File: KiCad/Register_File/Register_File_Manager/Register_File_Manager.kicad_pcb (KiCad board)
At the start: 2 copper layers, 100 x 100 mm, 39 parts, among them J1 Conn_01x04_Socket, J10 Conn_01x02_Socket, J11 Conn_01x02_Socket, J12 Conn_01x02_Socket, J13 Conn_01x02_Socket, J14 Conn_01x02_Socket, J15 Conn_01x02_Socket, J16 Conn_01x02_Socket, J17 Conn_01x02_Socket, J18 Conn_01x02_Socket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

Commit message: finished registier file boards
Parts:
- removed D0, D5, D6, D7: LED, LED_THT:LED_Rectangular_W3.0mm_H2.0mm
- removed RN1: R_Network08_US, Resistor_THT:R_Array_SIP9
- added J21: Conn_01x08_Socket, Connector_PinHeader_2.54mm:PinHeader_1x08_P2.54mm_Vertical, F.Cu at (142.3, 76.5)
- added J22: Conn_01x08_Socket, Connector_PinHeader_2.54mm:PinHeader_1x08_P2.54mm_Vertical, F.Cu at (177.4, 76.5)
- added J23: Conn_01x08_Socket, Connector_PinHeader_2.54mm:PinHeader_1x08_P2.54mm_Vertical, F.Cu at (142.9, 100.5)
- added J24: Conn_01x08_Socket, Connector_PinHeader_2.54mm:PinHeader_1x08_P2.54mm_Vertical, F.Cu at (176.1, 100.5)
- added R1: 1k, Resistor_SMD:R_1206_3216Metric_Pad1.30x1.75mm_HandSolder, F.Cu at (172.0, 60.5)
- added R2: 1k, Resistor_SMD:R_1206_3216Metric_Pad1.30x1.75mm_HandSolder, F.Cu at (176.0, 60.5)
- added R3: 1k, Resistor_SMD:R_1206_3216Metric_Pad1.30x1.75mm_HandSolder, F.Cu at (180.0, 60.5)
- added R4: 1k, Resistor_SMD:R_1206_3216Metric_Pad1.30x1.75mm_HandSolder, F.Cu at (184.0, 60.5)
- added SW1: SW_SPDT, Button_Switch_THT:SW_Slide_SPDT_Angled_CK_OS102011MA1Q, F.Cu at (117.5, 54.0)
- added U7: 74LS245, Package_DIP:DIP-20_W7.62mm_Socket_LongPads, F.Cu at (134.4, 63.8)
- moved D4 36.1 mm to (184.0, 54.0), turned to -90 degrees
- moved D3 24.6 mm to (180.0, 54.0), turned to -90 degrees
- moved U3 20.6 mm to (157.1, 87.8), turned to 90 degrees
- moved U5 16.0 mm to (155.8, 111.8), turned to 90 degrees
- moved J1 14.5 mm to (147.0, 142.0)
- moved J2 14.5 mm to (161.5, 142.0)
- moved D2 13.2 mm to (176.0, 54.0), turned to -90 degrees
- moved U2 12.9 mm to (122.0, 87.8), turned to 90 degrees
- moved U4 12.3 mm to (122.5, 111.8), turned to 90 degrees
- moved U1 7.07 mm to (155.6, 130.8)
- moved D1 2.50 mm to (172.0, 54.0), turned to -90 degrees
- moved U6 1.43 mm to (125.4, 131.2)
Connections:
- net /SELECTED_REG_0 renamed SELECTED_REG_0
- net /SELECTED_REG_1 renamed SELECTED_REG_1
- net /SELECTED_REG_2 renamed SELECTED_REG_2
- D1 pad 1: Net-(D1-K) -> GND
- D1 pad 2: unconnected-(D1-A-Pad2) -> Net-(D1-A)
- D2 pad 1: Net-(D2-K) -> GND
- D2 pad 2: unconnected-(D2-A-Pad2) -> Net-(D2-A)
- D3 pad 1: Net-(D3-K) -> GND
- D3 pad 2: unconnected-(D3-A-Pad2) -> Net-(D3-A)
- D4 pad 1: Net-(D4-K) -> GND
- D4 pad 2: unconnected-(D4-A-Pad2) -> Net-(D4-A)
- J4 pad 1: GND -> VCC
- J4 pad 2: VCC -> GND
- U1 pad 12: /SELECTED_REG_3 -> SELECTED_REG_3
- U2 pad 4: /SELECTED_REG_3_B -> SELECTED_REG_3
- U2 pad 5: /SELECTED_REG_3_B -> SELECTED_REG_3
- U3 pad 4: /SELECTED_REG_3 -> /SELECTED_REG_3_B
- U3 pad 5: /SELECTED_REG_3 -> /SELECTED_REG_3_B
- U4 pad 4: /SELECTED_REG_3_B -> SELECTED_REG_3
- U4 pad 5: /SELECTED_REG_3_B -> SELECTED_REG_3
- U5 pad 4: /SELECTED_REG_3 -> /SELECTED_REG_3_B
- U5 pad 5: /SELECTED_REG_3 -> /SELECTED_REG_3_B
- U6 pad 3: /SELECTED_REG_3 -> (no net)
- U6 pad 4: /SELECTED_REG_3_B -> (no net)
- U6 pad 8: (no net) -> /SELECTED_REG_3_B
- U6 pad 9: (no net) -> SELECTED_REG_3
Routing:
- net VCC: track 0.00 -> 257.6 mm, vias 0 -> 3
- net SELECTED_REG_3: track 0.00 -> 135.8 mm
- net /SELECTED_REG_3: track 90.8 -> 0.00 mm, vias 1 -> 0
- net SELECTED_REG_2: track 119.4 -> 199.9 mm, vias 2 -> 1
- net SELECTED_REG_1: track 122.9 -> 189.0 mm, vias 3 -> 1
- net SELECTED_REG_0: track 125.7 -> 175.9 mm, vias 3 -> 1
- net LED_2: track 0.00 -> 46.1 mm
- net LED_3: track 0.00 -> 45.9 mm
- net LED_1: track 0.00 -> 44.2 mm
- net LED_0: track 0.00 -> 40.5 mm
- net /IN_EN_REG_7: track 44.9 -> 76.7 mm
- net Net-(SW1-B): track 0.00 -> 26.3 mm
- net /OUT_EN_REG_7: track 30.0 -> 55.9 mm
- net /REG_SEL_DST_3: track 37.1 -> 62.0 mm
- net /REG_SEL_DST_2: track 28.5 -> 52.9 mm
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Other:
- board text added: "IN_0"
- board text added: "IN_1"
- board text added: "IN_10"
- board text added: "IN_11"
- board text added: "IN_12"
- board text added: "IN_13"
- board text added: "IN_14"
- board text added: "IN_15"
- board text added: "IN_2"
- board text added: "IN_3"
- board text added: "IN_4"
- board text added: "IN_5"
- board text added: "IN_6"
- board text added: "IN_7"
- board text added: "IN_8"
- board text added: "IN_9"
- board text added: "OUT_0"
- board text added: "OUT_1"
- board text added: "OUT_10"
- board text added: "OUT_11"
- board text added: "OUT_12"
- board text added: "OUT_13"
- board text added: "OUT_14"
- board text added: "OUT_15"
- board text added: "OUT_2"
- board text added: "OUT_3"
- board text added: "OUT_4"
- board text added: "OUT_5"
- board text added: "OUT_6"
- board text added: "OUT_7"
- board text added: "OUT_8"
- board text added: "OUT_9"
- board text added: "Register Manager"
- board text added: "SH8"
- board text added: "Selected Register"
- board text added: "rev 1.0"

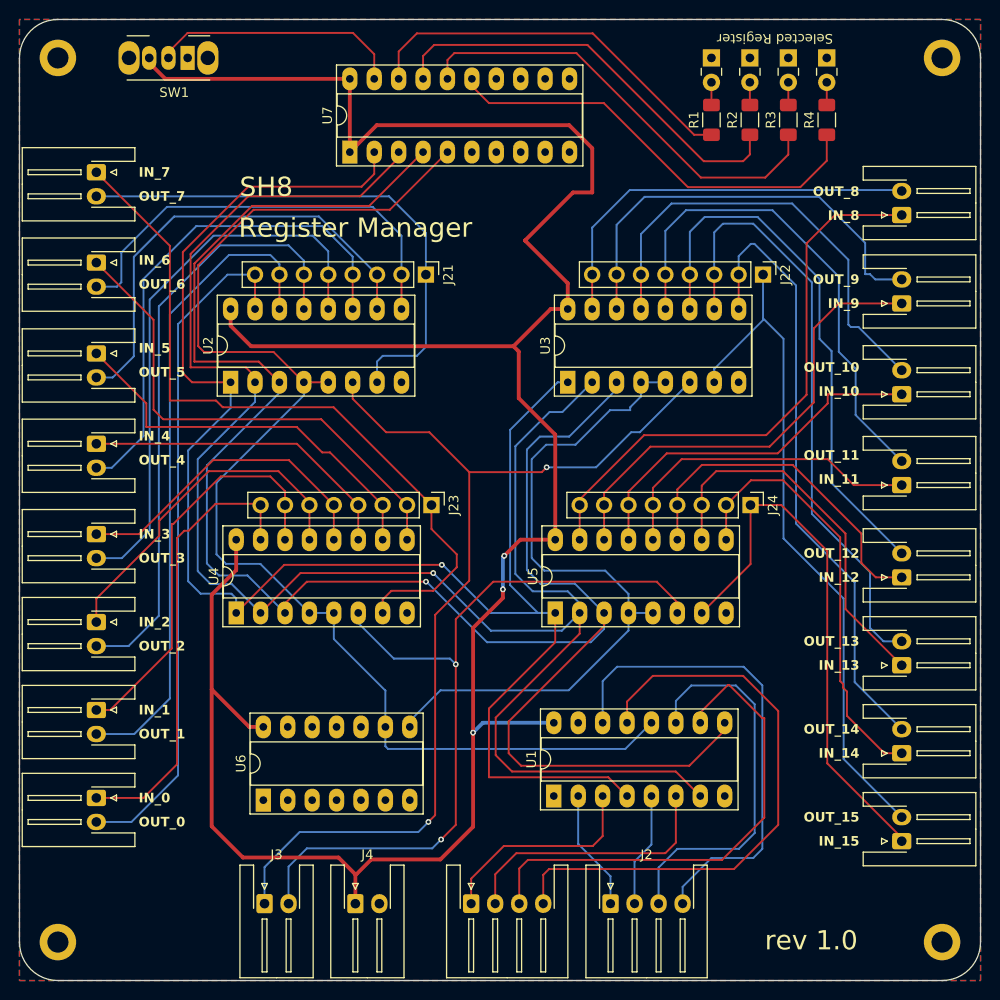
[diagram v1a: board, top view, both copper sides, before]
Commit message: added con_ctrl board mdr_mar
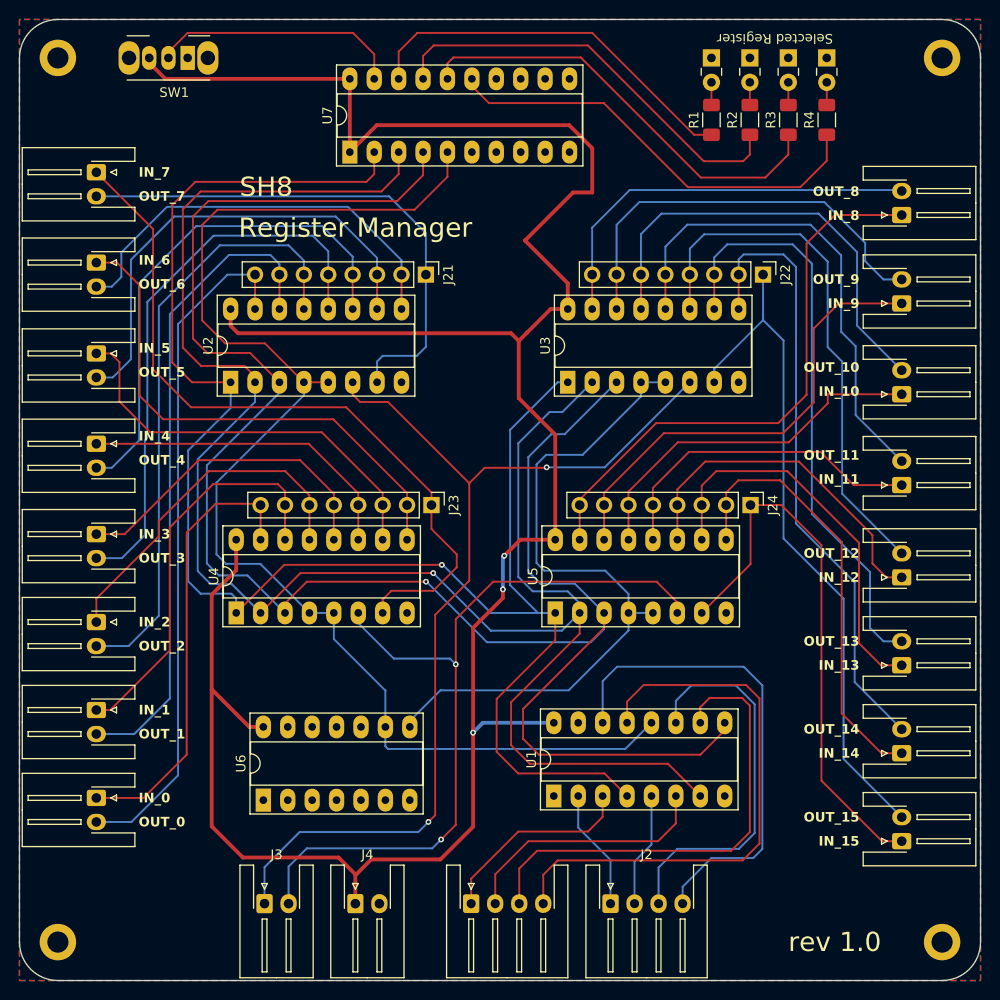
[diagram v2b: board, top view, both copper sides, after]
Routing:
- net /REG_SEL_DST_3: track 62.0 -> 59.2 mm
- net /OUT_EN_REG_13: track 63.4 -> 61.2 mm
- net /REG_SEL_DST_2: track 52.9 -> 50.7 mm
- net /IN_EN_REG_6: track 51.9 -> 53.8 mm
- net SELECTED_REG_2: track 199.9 -> 198.0 mm
- net /OUT_EN_REG_6: track 45.9 -> 44.1 mm
- net SELECTED_REG_0: track 175.9 -> 177.6 mm
- net /IN_EN_REG_5: track 41.4 -> 43.1 mm
- net SELECTED_REG_3: track 135.8 -> 137.3 mm
- net /IN_EN_REG_13: track 40.0 -> 41.5 mm
- net /OUT_EN_REG_9: track 45.1 -> 43.9 mm
- net /SELECTED_REG_3_B: track 73.8 -> 72.6 mm
- net /IN_EN_REG_15: track 56.7 -> 57.9 mm
- net /REG_SEL_DST_1: track 28.1 -> 26.9 mm
- net /REG_SEL_DST_0: track 22.3 -> 21.1 mm
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
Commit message: created standarts for PCB's
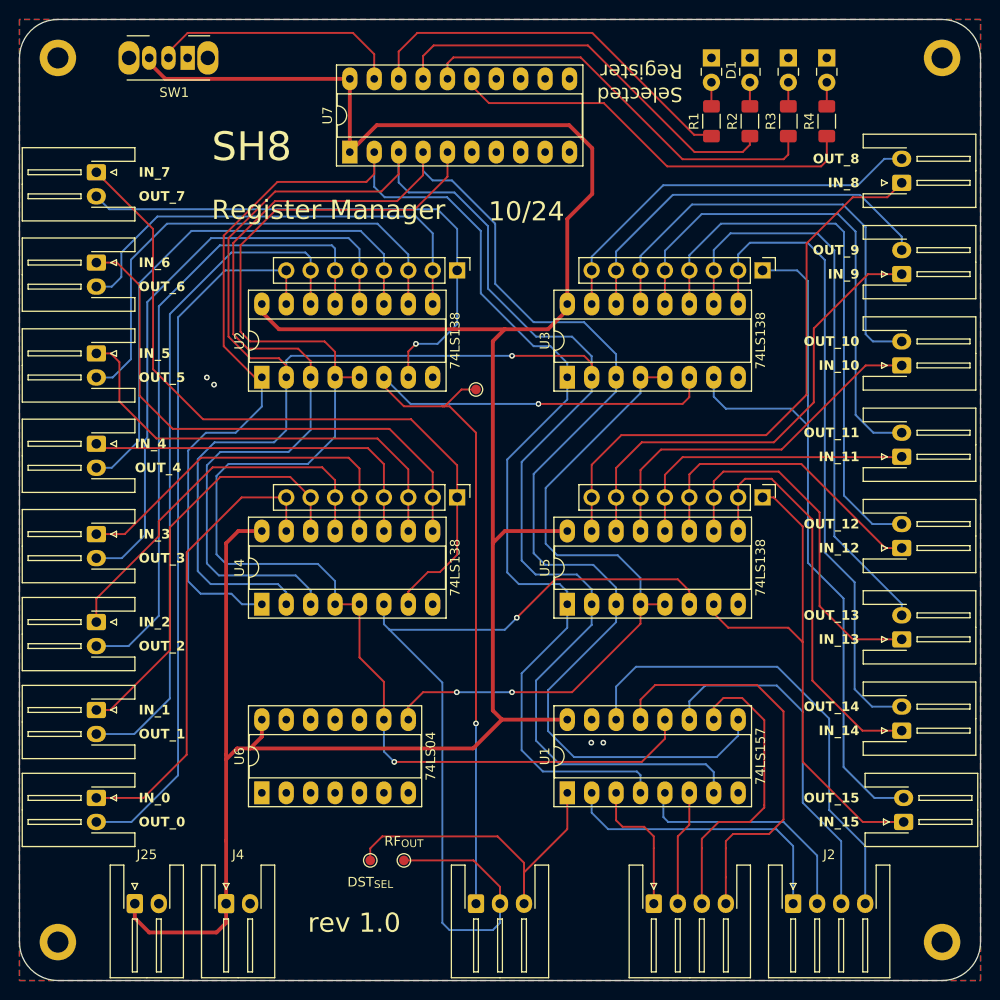
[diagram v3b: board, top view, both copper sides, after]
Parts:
- added J25: Conn_01x02_Socket, Connector_JST:JST_XH_S2B-XH-A-1_1x02_P2.50mm_Horizontal, F.Cu at (112.0, 142.0)
- added TP1: TestPoint, TestPoint:TestPoint_Pad_D1.0mm, F.Cu at (147.5, 88.5)
- added TP2: TestPoint, TestPoint:TestPoint_Pad_D1.0mm, F.Cu at (140.0, 137.5)
- added TP3: TestPoint, TestPoint:TestPoint_Pad_D1.0mm, F.Cu at (136.5, 137.5)
- J3: value Conn_01x02_Socket -> Conn_01x03_Socket; footprint Connector_JST:JST_XH_S2B-XH-A-1_1x02_P2.50mm_Horizontal -> Connector_JST:JST_XH_S3B-XH-A-1_1x03_P2.50mm_Horizontal
- moved J3 22.0 mm to (147.5, 142.0)
- moved J1 19.0 mm to (166.0, 142.0)
- moved J2 19.0 mm to (180.5, 142.0)
- moved J4 13.4 mm to (121.5, 142.0)
- moved J13 3.35 mm to (191.8, 67.0)
- moved U2 3.29 mm to (125.2, 87.2)
- moved J21 3.28 mm to (145.5, 76.1)
- moved J14 3.05 mm to (191.8, 76.5)
- moved J17 3.05 mm to (191.8, 105.0)
- moved J15 3.00 mm to (191.8, 86.0)
- moved J16 2.95 mm to (191.8, 95.5)
- moved U4 2.82 mm to (125.2, 110.8)
- moved J23 2.79 mm to (145.5, 99.7)
- moved J18 2.70 mm to (191.8, 114.5)
- moved J19 2.35 mm to (191.8, 124.0)
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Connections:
- net /RF_IN renamed RF_IN
- net /RF_OUT renamed RF_OUT
- U6 pad 1: (no net) -> GND
- U6 pad 10: (no net) -> unconnected-(U6-Pad10)
- U6 pad 11: (no net) -> GND
- U6 pad 12: (no net) -> unconnected-(U6-Pad12)
- U6 pad 13: (no net) -> GND
- U6 pad 2: (no net) -> unconnected-(U6-Pad2)
- U6 pad 3: (no net) -> GND
- U6 pad 4: (no net) -> unconnected-(U6-Pad4)
- U6 pad 5: (no net) -> GND
- U6 pad 6: (no net) -> unconnected-(U6-Pad6)
- U7 pad 11: LED_7 -> unconnected-(U7-B7-Pad11)
- U7 pad 12: LED_6 -> unconnected-(U7-B6-Pad12)
- U7 pad 13: LED_5 -> unconnected-(U7-B5-Pad13)
- U7 pad 14: LED_4 -> unconnected-(U7-B4-Pad14)
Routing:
- net DST_SEL: track 0.00 -> 35.1 mm
- net SELECTED_REG_1: track 190.0 -> 223.4 mm
- net /REG_SEL_DST_2: track 50.7 -> 31.6 mm
- net /REG_SEL_SRC_0: track 12.6 -> 30.5 mm
- net /REG_SEL_DST_3: track 59.2 -> 43.4 mm
- net /REG_SEL_DST_1: track 26.9 -> 12.0 mm
- net /REG_SEL_SRC_1: track 11.9 -> 25.3 mm
- net SELECTED_REG_3: track 137.3 -> 147.8 mm, vias 0 -> 1
- net RF_OUT: track 84.2 -> 92.5 mm, vias 2 -> 1
- net /REG_SEL_DST_0: track 21.1 -> 14.5 mm
- net /OUT_EN_REG_15: track 71.8 -> 77.9 mm
- net SELECTED_REG_0: track 177.6 -> 172.6 mm, vias 1 -> 0
- net /IN_EN_REG_12: track 36.5 -> 32.1 mm
- net /OUT_EN_REG_0: track 71.2 -> 74.9 mm
- net /IN_EN_REG_4: track 34.2 -> 37.8 mm
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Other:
- board text added: "10/24"
